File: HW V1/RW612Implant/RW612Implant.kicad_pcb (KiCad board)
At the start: 4 copper layers, 14 parts, among them IC1 RW612ET, IC2 SKY13323-378LF, U1 S25HS512TFANHI010, U2 APS6404L-3SQR-ZR, U3 SR4W035

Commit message: clocked up on a saturday
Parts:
- added C7: 2.2u, Capacitor_SMD:C_0201_0603Metric, F.Cu at (104.6, 97.8)
- added R1: 100R, Resistor_SMD:R_0201_0603Metric, F.Cu at (105.1, 93.8)
- added R2: 400R, Resistor_SMD:R_0201_0603Metric, F.Cu at (94.5, 100.2)
- added R3: 166R, Resistor_SMD:R_0201_0603Metric, F.Cu at (94.5, 99.4)
- added R4: 133R, Resistor_SMD:R_0201_0603Metric, F.Cu at (94.5, 100.9)
- added U4: IM67D128BV01, Library:PG-TLGA-5-8, F.Cu at (103.8, 98.6)
- added Y1: 616L3I040M00000R, Library:616L3I008M00000R, F.Cu at (104.5, 96.3)
- moved U1 0.75 mm to (93.2, 94.7)
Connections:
- IC1 pad A10: unconnected-(IC1-VBAT_1-PadA10) -> +3V3
- IC1 pad A4: unconnected-(IC1-VIO_5-PadA4) -> +3V3
- IC1 pad B10: unconnected-(IC1-VBAT_2-PadB10) -> +3V3
- IC1 pad B12: unconnected-(IC1-AVDD18_1-PadB12) -> +1V8
- IC1 pad D1: unconnected-(IC1-VIO_4-PadD1) -> +1V8
- IC1 pad F14: unconnected-(IC1-AVDD18_2-PadF14) -> +1V8
- IC1 pad F15: unconnected-(IC1-AVDD18_3-PadF15) -> +1V8
- IC1 pad G15: unconnected-(IC1-XTAL_OUT-PadG15) -> Net-(IC1-XTAL_OUT)
- IC1 pad H15: unconnected-(IC1-XTAL_IN-PadH15) -> Net-(IC1-XTAL_IN)
- IC1 pad J15: unconnected-(IC1-AVDD18_4-PadJ15) -> +1V8
- IC1 pad K1: unconnected-(IC1-VIO_1-PadK1) -> +1V8
- IC1 pad K15: unconnected-(IC1-AVDD18_5-PadK15) -> +1V8
- IC1 pad L15: unconnected-(IC1-AVDD18_6-PadL15) -> +1V8
- IC1 pad M15: unconnected-(IC1-AVDD18_7-PadM15) -> +1V8
- IC1 pad N15: unconnected-(IC1-AVDD18_8-PadN15) -> +1V8
- IC1 pad P1: unconnected-(IC1-AVDD18_9-PadP1) -> +1V8
- IC1 pad R1: unconnected-(IC1-AVDD18_10-PadR1) -> +1V8
- IC1 pad R10: unconnected-(IC1-AVDD18_12-PadR10) -> +1V8
- IC1 pad R11: unconnected-(IC1-AVDD18_13-PadR11) -> +1V8
- IC1 pad R12: unconnected-(IC1-AVDD18_14-PadR12) -> +1V8
- IC1 pad R2: unconnected-(IC1-AVDD18_11-PadR2) -> +1V8
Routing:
- net +1V8: track 0.00 -> 19.7 mm, vias 0 -> 15
- net /Storage/FLASH_D1: track 0.00 -> 19.1 mm, vias 0 -> 2
- net /Storage/FLASH_D3: track 0.45 -> 19.2 mm, vias 1 -> 2
- net /Storage/FLASH_D2: track 0.45 -> 19.1 mm, vias 1 -> 2
- net /Storage/~{FLASH_CS}: track 0.50 -> 19.2 mm, vias 1 -> 2
- net /Storage/FLASH_CLK: track 0.50 -> 19.1 mm, vias 1 -> 2
- net /Storage/FLASH_D0: track 0.71 -> 19.2 mm, vias 1 -> 2
- net /Peripherals/MIC_D: track 0.00 -> 12.8 mm, vias 0 -> 2
- net /Peripherals/MIC_C: track 0.00 -> 11.8 mm, vias 0 -> 2
- net Net-(IC1-XTAL_IN): track 0.00 -> 7.93 mm
- net Net-(IC1-XTAL_OUT): track 0.00 -> 5.95 mm
- net GND: track 36.5 -> 38.7 mm, vias 87 -> 72
- net +3V3: track 0.00 -> 1.00 mm, vias 0 -> 1
- added copper zone on In2.Cu, net +1V8
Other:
- board outline added: 15.7 x 22.2 mm
- board text removed: "mic"

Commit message: we do a little routing
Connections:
- IC1 pad A5: unconnected-(IC1-VIO_3-PadA5) -> +3V3
- IC1 pad B15: unconnected-(IC1-VIO_6-PadB15) -> +3V3
- IC1 pad C5: unconnected-(IC1-GPIO[27]-PadC5) -> LED_G
- IC1 pad F6: unconnected-(IC1-GPIO[26]-PadF6) -> LED_R
- IC1 pad F8: unconnected-(IC1-GPIO[4]-PadF8) -> LED_B
- R2 pad 1: /Peripherals/LED_R -> LED_R
- R3 pad 1: /Peripherals/LED_G -> LED_G
- R4 pad 1: /Peripherals/LED_B -> LED_B
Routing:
- net LED_B: track 0.00 -> 16.8 mm, vias 0 -> 2
- net LED_G: track 0.00 -> 16.6 mm, vias 0 -> 2
- net LED_R: track 0.00 -> 16.1 mm, vias 0 -> 2
- net +3V3: track 1.00 -> 7.91 mm, vias 1 -> 3
- net +1V8: track 19.7 -> 21.3 mm, vias 15 -> 16
- net GND: track 38.7 -> 37.7 mm, vias 72 -> 69

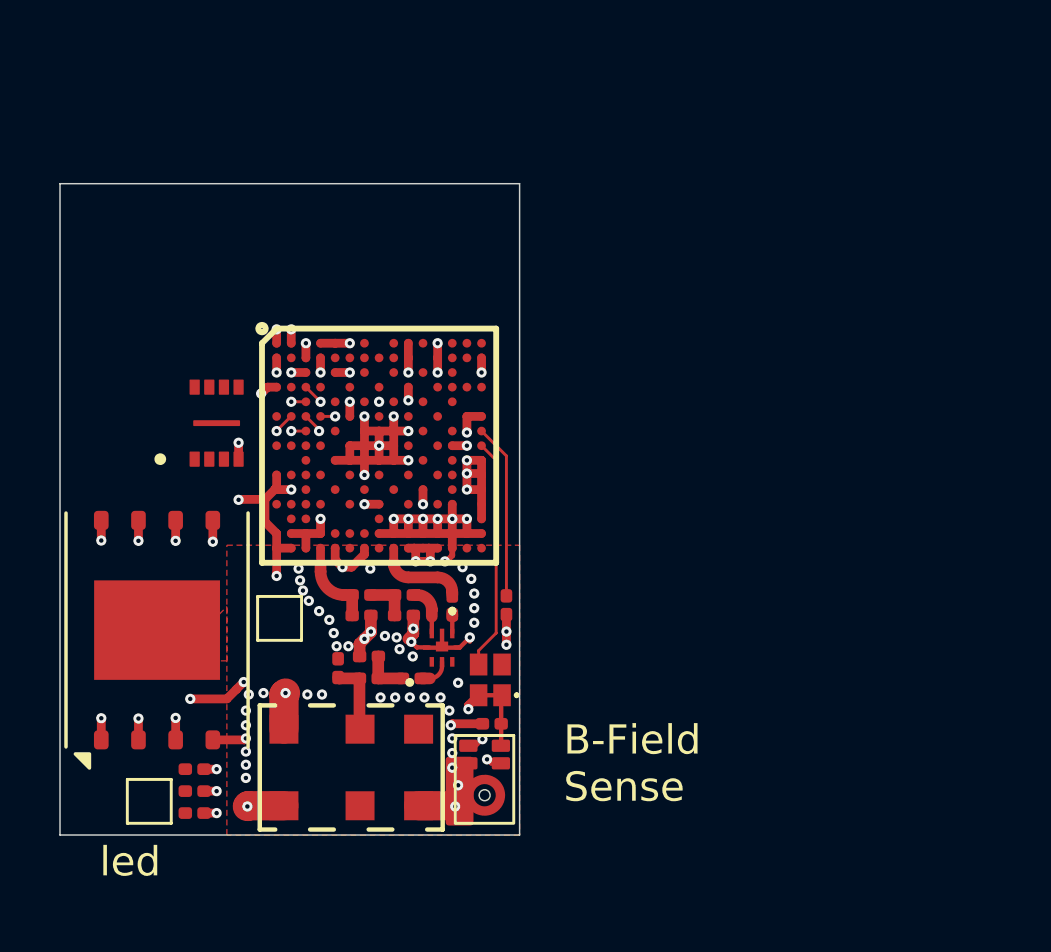
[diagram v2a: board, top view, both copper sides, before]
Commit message: we do a little led routing
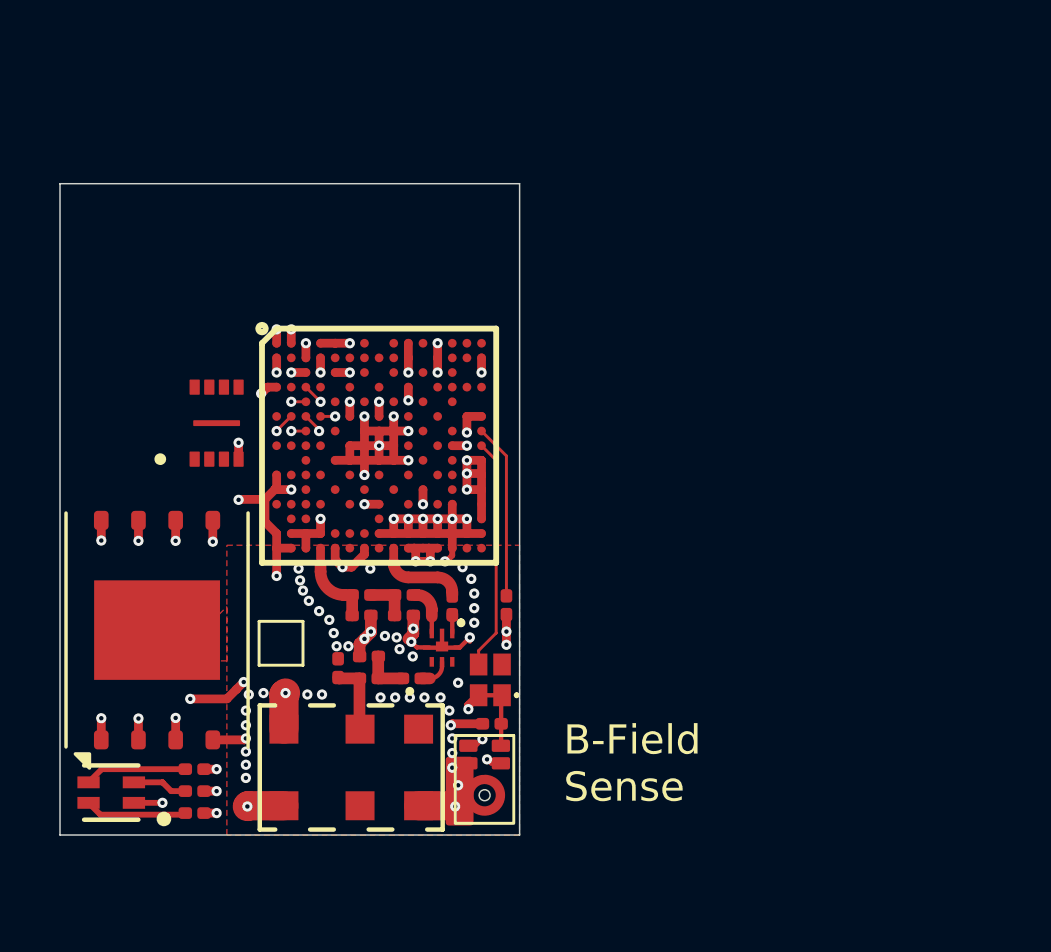
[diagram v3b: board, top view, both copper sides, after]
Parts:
- added LED1: CLMUD-FKC-CHJNPM569ABB845343, Library:PLCC4_CLMUD-FKC_CRW, F.Cu at (91.6, 100.2)
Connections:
- R2 pad 2: unconnected-(R2-Pad2) -> Net-(LED1-CATHODE_RED)
- R3 pad 2: unconnected-(R3-Pad2) -> Net-(LED1-CATHODE_GREEN)
- R4 pad 2: unconnected-(R4-Pad2) -> Net-(LED1-CATHODE_BLUE)
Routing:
- net +3V3: track 7.91 -> 23.1 mm, vias 3 -> 4
- net Net-(LED1-CATHODE_BLUE): track 0.00 -> 3.49 mm
- net Net-(LED1-CATHODE_GREEN): track 0.00 -> 3.49 mm
- net Net-(LED1-CATHODE_RED): track 0.00 -> 1.88 mm
- net LED_B: track 16.8 -> 17.3 mm
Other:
- board text removed: "led"

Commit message: everything except temp and qi?
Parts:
- added C10: 0.1u, Capacitor_SMD:C_0201_0603Metric, F.Cu at (95.0, 89.0)
- added C11: 0.1u, Capacitor_SMD:C_0201_0603Metric, F.Cu at (95.0, 89.8)
- added C12: 0.1u, Capacitor_SMD:C_0201_0603Metric, F.Cu at (95.0, 88.2)
- added C13: 0.1u, Capacitor_SMD:C_0201_0603Metric, F.Cu at (103.5, 94.1)
- added C14: 0.1u, Capacitor_SMD:C_0201_0603Metric, F.Cu at (95.0, 84.8)
- added C15: 100p, Capacitor_SMD:C_0201_0603Metric, F.Cu at (105.0, 94.1)
- added C16: 0.1u, Capacitor_SMD:C_0201_0603Metric, F.Cu at (95.0, 85.5)
- added C17: 0.1u, Capacitor_SMD:C_0201_0603Metric, F.Cu at (95.0, 86.5)
- added C18: 470p, Capacitor_SMD:C_0201_0603Metric, F.Cu at (95.0, 87.2)
- added C19: 6TPS150MUD, Capacitor_Tantalum_SMD:CP_EIA-3528-21_Kemet-B, F.Cu at (91.5, 82.8)
- added C20: 6TPS150MUD, Capacitor_Tantalum_SMD:CP_EIA-3528-21_Kemet-B, F.Cu at (91.5, 87.8)
- added C21: 22u X5R 6.3V, Capacitor_SMD:C_0402_1005Metric, F.Cu at (93.8, 85.5)
- added C22: 22u X5R 6.3V, Capacitor_SMD:C_0402_1005Metric, F.Cu at (93.8, 89.3)
- added C24: 22u X5R 6.3V, Capacitor_SMD:C_0402_1005Metric, F.Cu at (93.8, 87.4)
- added C25: 0.1u, Capacitor_SMD:C_0201_0603Metric, F.Cu at (104.1, 82.6)
- added C26: 470p, Capacitor_SMD:C_0201_0603Metric, F.Cu at (104.8, 82.6)
- added C27: 0.1u, Capacitor_SMD:C_0201_0603Metric, F.Cu at (98.0, 82.6)
- added C28: 0.1u, Capacitor_SMD:C_0201_0603Metric, F.Cu at (98.0, 80.4)
- added C29: 0.1u, Capacitor_SMD:C_0201_0603Metric, F.Cu at (98.3, 81.5)
- added C30: 0.1u, Capacitor_SMD:C_0201_0603Metric, F.Cu at (103.3, 82.6)
- added C31: 22u X5R 6.3V, Capacitor_SMD:C_0402_1005Metric, F.Cu at (104.1, 80.3)
- added C32: 22u X5R 6.3V, Capacitor_SMD:C_0402_1005Metric, F.Cu at (104.1, 81.3)
- added C8: 0.1u, Capacitor_SMD:C_0201_0603Metric, F.Cu at (95.0, 84.1)
- added IC3: NMH1000T1, Library:NMH1000T1, F.Cu at (97.9, 95.1)
- added J1: Conn_ARM_SWD_TagConnect_TC2030-NL, Connector:Tag-Connect_TC2030-IDC-NL_2x03_P1.27mm_Vertical, B.Cu at (96.3, 81.6)
- added L4: LQM21PN1R0NGRD, Inductor_SMD:L_0805_2012Metric, F.Cu at (100.3, 81.5)
- added L5: LQM21PN1R0NGRD, Inductor_SMD:L_0805_2012Metric, F.Cu at (102.1, 81.5)
- added R5: 50R, Resistor_SMD:R_0201_0603Metric, F.Cu at (104.3, 94.1)
- added R6: 51k, Resistor_SMD:R_0201_0603Metric, F.Cu at (94.0, 80.5)
- LED1: value CLMUD-FKC-CHJNPM569ABB845343 -> CLMUD-FKC
- U1: footprint Library:WSON-8-1EP_8x6mm_P1.27mm_EP3.4x4.3mm -> Package_SON:WSON-8-1EP_8x6mm_P1.27mm_EP3.4x4.3mm
- moved R1 15.2 mm to (93.8, 83.8), turned to 90 degrees
- moved U2 6.09 mm to (96.2, 81.6), turned to -90 degrees
- moved C5 0.82 mm to (101.1, 96.6)
- moved C6 0.80 mm to (99.7, 96.6)
- moved L2 0.76 mm to (101.1, 95.8), turned to 0 degrees
- moved IC2 0.64 mm to (102.6, 95.8)
- moved C1 0.50 mm to (102.8, 94.1)
- moved L3 0.32 mm to (99.7, 95.8), turned to 0 degrees
- moved C2 0.32 mm to (100.0, 94.4)
- moved L1 0.32 mm to (100.0, 93.7)
- moved C3 0.32 mm to (101.4, 94.4)
- moved C4 0.32 mm to (101.4, 93.7)
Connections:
- IC1 pad A11: unconnected-(IC1-BUCK18_VOUT-PadA11) -> Net-(IC1-BUCK18_VOUT)
- IC1 pad A14: unconnected-(IC1-GPIO[56]-PadA14) -> I2C_SCL
- IC1 pad A9: unconnected-(IC1-BUCK11_VOUT-PadA9) -> Net-(IC1-BUCK11_VOUT)
- IC1 pad B13: unconnected-(IC1-GPIO[57]-PadB13) -> I2C_SDA
- IC1 pad B8: unconnected-(IC1-AVDD33_USB-PadB8) -> +3V3
- IC1 pad B9: unconnected-(IC1-BUCK11_SENSE-PadB9) -> +1V0
- IC1 pad C11: unconnected-(IC1-BUCK18_SENSE-PadC11) -> +1V8
- IC1 pad D15: unconnected-(IC1-VCORE_2-PadD15) -> +1V0
- IC1 pad D4: unconnected-(IC1-VCORE_1-PadD4) -> +1V0
- IC1 pad E9: unconnected-(IC1-PDN-PadE9) -> ~{RESET}
- IC1 pad F1: unconnected-(IC1-VIO_2-PadF1) -> +3V3
- IC1 pad G5: unconnected-(IC1-GPIO[13]-PadG5) -> SWCLK
- IC1 pad H1: unconnected-(IC1-VCORE_3-PadH1) -> +1V0
- IC1 pad J13: unconnected-(IC1-EXT_FREQ/WCI-2_SOUT-PadJ13) -> +1V8
- IC1 pad K10: unconnected-(IC1-VCORE_4-PadK10) -> +1V0
- IC1 pad K13: unconnected-(IC1-EXT_PRI-PadK13) -> +1V8
- IC1 pad K4: unconnected-(IC1-GPIO[14]-PadK4) -> SWDIO
- IC1 pad K6: unconnected-(IC1-GPIO[55]-PadK6) -> /Peripherals/B_SWITCH
- IC1 pad L13: unconnected-(IC1-EXT_GNT-PadL13) -> +1V8
- IC1 pad M12: unconnected-(IC1-EXT_REQ-PadM12) -> +1V8
- IC1 pad N3: unconnected-(IC1-RF_CNTL0-PadN3) -> /RF/RF_CNTL_0
- IC1 pad P5: unconnected-(IC1-RF_CNTL1-PadP5) -> /RF/RF_CNTL_1
- IC1 pad P6: unconnected-(IC1-RF_CNTL2-PadP6) -> GND
- IC1 pad R14: unconnected-(IC1-RF_TR_5-PadR14) -> Net-(IC1-RF_TR_5)
- IC1 pad R15: unconnected-(IC1-VPA_2-PadR15) -> +3V3
- IC1 pad R6: unconnected-(IC1-VIO_RF-PadR6) -> +1V8
- IC1 pad R8: unconnected-(IC1-VPA_1-PadR8) -> +3V3
- IC2 pad 4: /RF/VCTL2 -> /RF/RF_CNTL_1
- IC2 pad 6: /RF/VCTL1 -> /RF/RF_CNTL_0
- U2 pad 8: +3.3V -> +3V3
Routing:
- net +3V3: track 23.1 -> 78.9 mm, vias 4 -> 11
- net +1V0: track 0.00 -> 32.5 mm, vias 0 -> 7
- net GND: track 37.7 -> 61.4 mm, vias 69 -> 54
- net ~{RESET}: track 0.00 -> 22.2 mm, vias 0 -> 3
- net +1V8: track 21.3 -> 43.3 mm, vias 16 -> 22
- net SWCLK: track 0.00 -> 21.8 mm, vias 0 -> 3
- net SWDIO: track 0.00 -> 19.4 mm, vias 0 -> 3
- net /RF/RF_CNTL_1: track 0.00 -> 12.7 mm, vias 0 -> 2
- net /RF/RF_CNTL_0: track 0.00 -> 10.3 mm, vias 0 -> 2
- net Net-(IC1-XTAL_OUT): track 5.95 -> 14.2 mm, vias 0 -> 2
- net /Storage/~{RAM_CS}: track 0.50 -> 7.88 mm, vias 1 -> 2
- net /Storage/RAM_D2: track 0.47 -> 7.85 mm, vias 1 -> 2
- net /Storage/RAM_CLK: track 0.50 -> 7.88 mm, vias 1 -> 2
- net /Storage/RAM_D1: track 0.47 -> 7.84 mm, vias 1 -> 2
- net /Storage/RAM_D0: track 0.50 -> 7.85 mm, vias 1 -> 2
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- added copper zone on B.Cu, net +1V8
- removed copper zone on In2.Cu, net +1V8
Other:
- board size 15.7 x 22.2 mm -> 15.7 x 26.5 mm
- board text removed: "B-Field Sense"

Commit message: gods greatest decoupler
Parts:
- added C23: 0.1u, Capacitor_SMD:C_0201_0603Metric, F.Cu at (105.3, 89.8)
- added C33: 0.1u, Capacitor_SMD:C_0201_0603Metric, F.Cu at (105.3, 88.4)
- added C34: 0.1u, Capacitor_SMD:C_0201_0603Metric, F.Cu at (105.3, 87.0)
- added C35: 0.1u, Capacitor_SMD:C_0201_0603Metric, F.Cu at (100.2, 93.0)
- added C36: 0.1u, Capacitor_SMD:C_0201_0603Metric, F.Cu at (105.3, 91.3)
- added C9: 470p, Capacitor_SMD:C_0201_0603Metric, F.Cu at (105.3, 85.5)
- added R7: 51k, Resistor_SMD:R_0201_0603Metric, F.Cu at (91.6, 100.2)
- added R8: 51k, Resistor_SMD:R_0201_0603Metric, F.Cu at (92.1, 80.0)
- added R9: 51k, Resistor_SMD:R_0201_0603Metric, F.Cu at (90.7, 80.0)
- C5: value 5.6pf -> 0.1u
- LED1, U3: moved to B.Cu
- moved C5 13.2 mm to (105.3, 84.0), turned to -90 degrees
- moved C6 1.09 mm to (100.8, 96.6)
- moved U4 0.16 mm to (104.0, 98.7)
- turned C19 to -90 degrees
- turned L3 to 180 degrees
- turned LED1 to 0 degrees
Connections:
- C19 pad 1: +3V3 -> +5V
- C5 pad 1: Net-(C5-Pad1) -> +1V0
- C5 pad 2: Net-(IC2-INPUT) -> GND
- C6 pad 2: Net-(C5-Pad1) -> Net-(IC2-INPUT)
- IC1 pad F12: unconnected-(IC1-GPIO[46]-PadF12) -> Net-(IC1-GPIO[46])
- IC1 pad P6: GND -> Net-(IC1-RF_CNTL2)
- L2 pad 1: Net-(C5-Pad1) -> Net-(IC2-INPUT)
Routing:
- net Net-(IC1-RF_CNTL2): track 0.00 -> 19.9 mm, vias 0 -> 2
- net Net-(IC1-GPIO[46]): track 0.00 -> 19.0 mm, vias 0 -> 2
- net +1V8: track 43.3 -> 47.8 mm, vias 22 -> 21
- net Net-(LED1-R): track 1.88 -> 5.36 mm, vias 0 -> 1
- net +5V: track 0.00 -> 1.72 mm
- net Net-(C5-Pad1): track 1.56 -> 0.00 mm
- net Net-(LED1-B): track 3.49 -> 1.98 mm, vias 0 -> 1
- net +3V3: track 78.9 -> 77.5 mm, vias 11 -> 10
- net Net-(LED1-G): track 3.49 -> 2.15 mm, vias 0 -> 1
- net Net-(IC2-INPUT): track 1.61 -> 2.84 mm
- net +1V0: track 32.5 -> 33.5 mm
- net GND: track 61.4 -> 62.1 mm, vias 54 -> 59
- net Net-(U3-FEED): track 2.54 -> 2.98 mm, vias 0 -> 1
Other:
- board size 15.7 x 26.5 mm -> 16 x 26.5 mm
